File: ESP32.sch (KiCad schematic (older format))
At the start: 30 parts, among them J201 GPIO, J202 Power, J203 Conn_01x01, J206 IO, J207 Conn_01x07, U201 ESP32-WROOM-32D

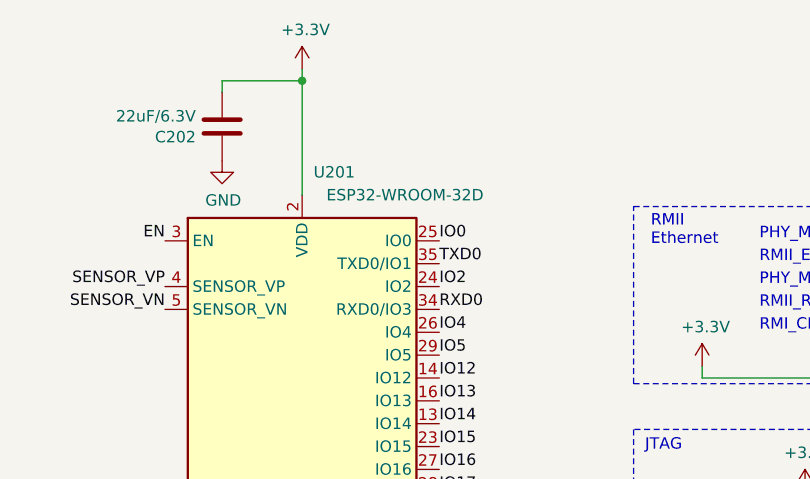
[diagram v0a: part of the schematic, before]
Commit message: - Fixed LCSC part number of USB Connector - Change CPU to ESP32-WROOM32E  part (was D)  and fixed LCSC part number - Fixed Name / silkscreen for Blank Tempalte
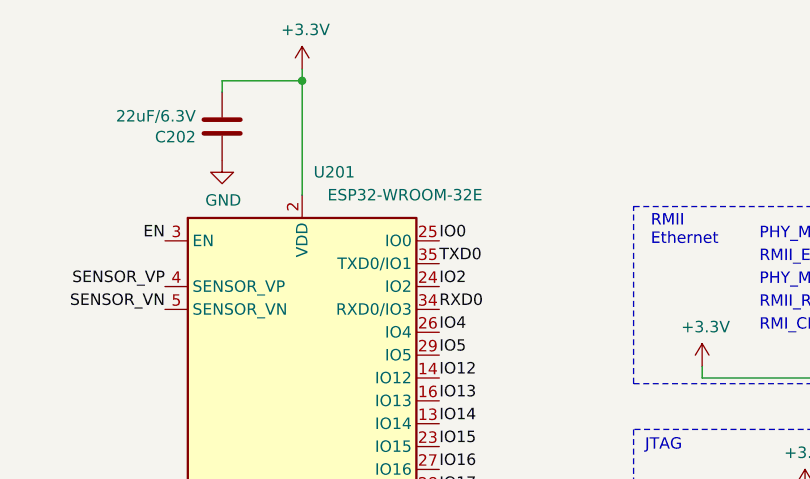
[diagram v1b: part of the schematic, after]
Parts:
- U201: value ESP32-WROOM-32D -> ESP32-WROOM-32E; LCSC C82899 -> C701341
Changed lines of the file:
@@
 AR Path="/5FC3847D/5FC47E0F" Ref="U201"  Part="1"
 F 0 "U201" H 2600 4400 50  0000 L CNN
-F 1 "ESP32-WROOM-32D" H 3000 4300 50  0000 C CNN
+F 1 "ESP32-WROOM-32E" H 3000 4300 50  0000 C CNN
 F 2 "RF_Module:ESP32-WROOM-32" H 2550 1400 50  0001 C CNN
 F 3 "https://www.espressif.com/sites/default/files/documentation/esp32-wroom-32d_esp32-wroom-32u_datasheet_en.pdf" H 2250 2950 50  0001 C CNN
-F 4 "C82899" H 2550 2900 50  0001 C CNN "LCSC"
+F 4 "C701341" H 2550 2900 50  0001 C CNN "LCSC"
 	1    2550 2900
 	1    0    0    -1

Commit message: Update pin header LCSC part numbers
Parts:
- J201: LCSC C358701 -> C429965
- J202: LCSC C358699 -> C65114
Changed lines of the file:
@@
 F 2 "Connector_PinHeader_2.54mm:PinHeader_2x03_P2.54mm_Vertical" H 9350 5225 50  0001 C CNN
 F 3 "~" H 9350 5225 50  0001 C CNN
-F 4 "C358699" H 9350 5225 50  0001 C CNN "LCSC"
+F 4 "C65114" H 9350 5225 50  0001 C CNN "LCSC"
 	1    9350 5225
 	1    0    0    -1
@@
 F 2 "Connector_PinHeader_2.54mm:PinHeader_2x20_P2.54mm_Vertical" H 5450 2600 50  0001 C CNN
 F 3 "~" H 5450 2600 50  0001 C CNN
-F 4 "C358701" H 5450 2600 50  0001 C CNN "LCSC"
+F 4 "C429965" H 5450 2600 50  0001 C CNN "LCSC"
 	1    5450 2600
 	1    0    0    -1

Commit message: Modify ESP32 footprint for Hand Soldering - Extended all pads 1mm outwards - Rearranged 0-Ohm links and EN/CLK area for new footprint - Added 3V3 and GND pads to corners of Prototype Area - Tidied up Silkscreen
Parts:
- U201: footprint RF_Module:ESP32-WROOM-32 -> SH-ESP32:ESP32-WROOM-32-HandSolder
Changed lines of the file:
@@
 F 0 "U201" H 2600 4400 50  0000 L CNN
 F 1 "ESP32-WROOM-32E" H 3000 4300 50  0000 C CNN
-F 2 "RF_Module:ESP32-WROOM-32" H 2550 1400 50  0001 C CNN
+F 2 "SH-ESP32:ESP32-WROOM-32-HandSolder" H 2550 1400 50  0001 C CNN
 F 3 "https://www.espressif.com/sites/default/files/documentation/esp32-wroom-32d_esp32-wroom-32u_datasheet_en.pdf" H 2250 2950 50  0001 C CNN
 F 4 "C701341" H 2550 2900 50  0001 C CNN "LCSC"

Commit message: Power system bug fix. Changed fuses & Diode - Swapping incorrect part  D1101 and D1102  to BAT54A   /  LCSC:  C83936 -Removed Perfect Diode, replaced with B5819W  Schottky - Replaced USB PTC Fuse ( F401 ) with   ASMD1206-050  /   C135338 - Replaced VIN ( F301 ) & CAN (F601 )PTC Fuses with  mSMD050-60V  / C70113 - Rerouted power and CAN power areas of board. - Removed all perfectDiode components/tracks and replaced with Schottky
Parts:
- D1101, D1102: LCSC C134407 -> C83936
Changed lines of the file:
@@
 $Descr A4 11693 8268
 encoding utf-8
-Sheet 11 11
+Sheet 11 10
 Title "Sailor Hat for ESP32"
 Date "2020-11-25"
@@
 F 1 "BAT54A" V 1895 5587 50  0000 L CNN
 F 2 "Package_TO_SOT_SMD:SOT-523" H 1925 5625 50  0001 L CNN
-F 3 "http://www.diodes.com/_files/datasheets/ds11005.pdf" H 1730 5500 50  0001 C CNN
-F 4 "C134407" V 1850 5500 50  0001 C CNN "LCSC"
+F 3 "https://datasheet.lcsc.com/szlcsc/Semtech-BAT54A_C83936.pdf" H 1730 5500 50  0001 C CNN
+F 4 "C83936" V 1850 5500 50  0001 C CNN "LCSC"
 	1    1850 5500
 	0    -1   1    0
@@
 F 1 "BAT54A" V 1805 6837 50  0000 L CNN
 F 2 "Package_TO_SOT_SMD:SOT-523" H 1925 6875 50  0001 L CNN
-F 3 "http://www.diodes.com/_files/datasheets/ds11005.pdf" H 1730 6750 50  0001 C CNN
-F 4 "C134407" V 1850 6750 50  0001 C CNN "LCSC"
+F 3 "https://datasheet.lcsc.com/szlcsc/Semtech-BAT54A_C83936.pdf" H 1730 6750 50  0001 C CNN
+F 4 "C83936" V 1850 6750 50  0001 C CNN "LCSC"
 	1    1850 6750
 	0    -1   -1   0
@@
 F 4 "C25744" H 2300 5300 50  0001 C CNN "LCSC"
 	1    2300 5300
-	1    0    0    -1
-$EndComp
-$Comp
-L power:+3.3V #PWR?
-U 1 1 5FBDFE88
-P 2300 5100
-AR Path="/5FBDFE88" Ref="#PWR?"  Part="1"
-AR Path="/5FC3847D/5FBDFE88" Ref="#PWR0102"  Part="1"
-F 0 "#PWR0102" H 2300 4950 50  0001 C CNN
-F 1 "+3.3V" H 2315 5273 50  0000 C CNN
-F 2 "" H 2300 5100 50  0001 C CNN
-F 3 "" H 2300 5100 50  0001 C CNN
-	1    2300 5100
 	1    0    0    -1
 $EndComp
@@
 Wire Wire Line
 	4900 2600 5250 2600
-Connection ~ 2300 5100
 Wire Notes Line
 	4000 2325 6750 2325

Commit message: Fix D1101 and D1102 part numbers
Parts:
- D1101, D1102: LCSC C83936 -> C134403
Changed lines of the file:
@@
 F 1 "BAT54A" V 1895 5587 50  0000 L CNN
 F 2 "Package_TO_SOT_SMD:SOT-523" H 1925 5625 50  0001 L CNN
-F 3 "https://datasheet.lcsc.com/szlcsc/Semtech-BAT54A_C83936.pdf" H 1730 5500 50  0001 C CNN
-F 4 "C83936" V 1850 5500 50  0001 C CNN "LCSC"
+F 3 "" H 1730 5500 50  0001 C CNN
+F 4 "C134403" V 1850 5500 50  0001 C CNN "LCSC"
 	1    1850 5500
 	0    -1   1    0
@@
 F 1 "BAT54A" V 1805 6837 50  0000 L CNN
 F 2 "Package_TO_SOT_SMD:SOT-523" H 1925 6875 50  0001 L CNN
-F 3 "https://datasheet.lcsc.com/szlcsc/Semtech-BAT54A_C83936.pdf" H 1730 6750 50  0001 C CNN
-F 4 "C83936" V 1850 6750 50  0001 C CNN "LCSC"
+F 3 "" H 1730 6750 50  0001 C CNN
+F 4 "C134403" V 1850 6750 50  0001 C CNN "LCSC"
 	1    1850 6750
 	0    -1   -1   0
